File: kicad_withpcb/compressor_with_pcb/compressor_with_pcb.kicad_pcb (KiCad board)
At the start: 2 copper layers, 152.3 x 105 mm, 166 parts, among them J1 EDA 306, Q1 BC549C, Q2 BC549C, Q3 BC549C, Q4 BC549C, Q5 BC549C, Q6 BC549C, Q7 BC549C, Q8 BC549C, Q9 BC549C, SW1 BYPASS, SW2 INT/EXT, SW3 HPF DEFEAT, SW4 LINK, U1 NE5532, U10 LM3915, U2 NE5532, U3 NE5532, U4 TL072, U5 NE5532, U6 NE5532, U7 NE5532, U9 LM3914

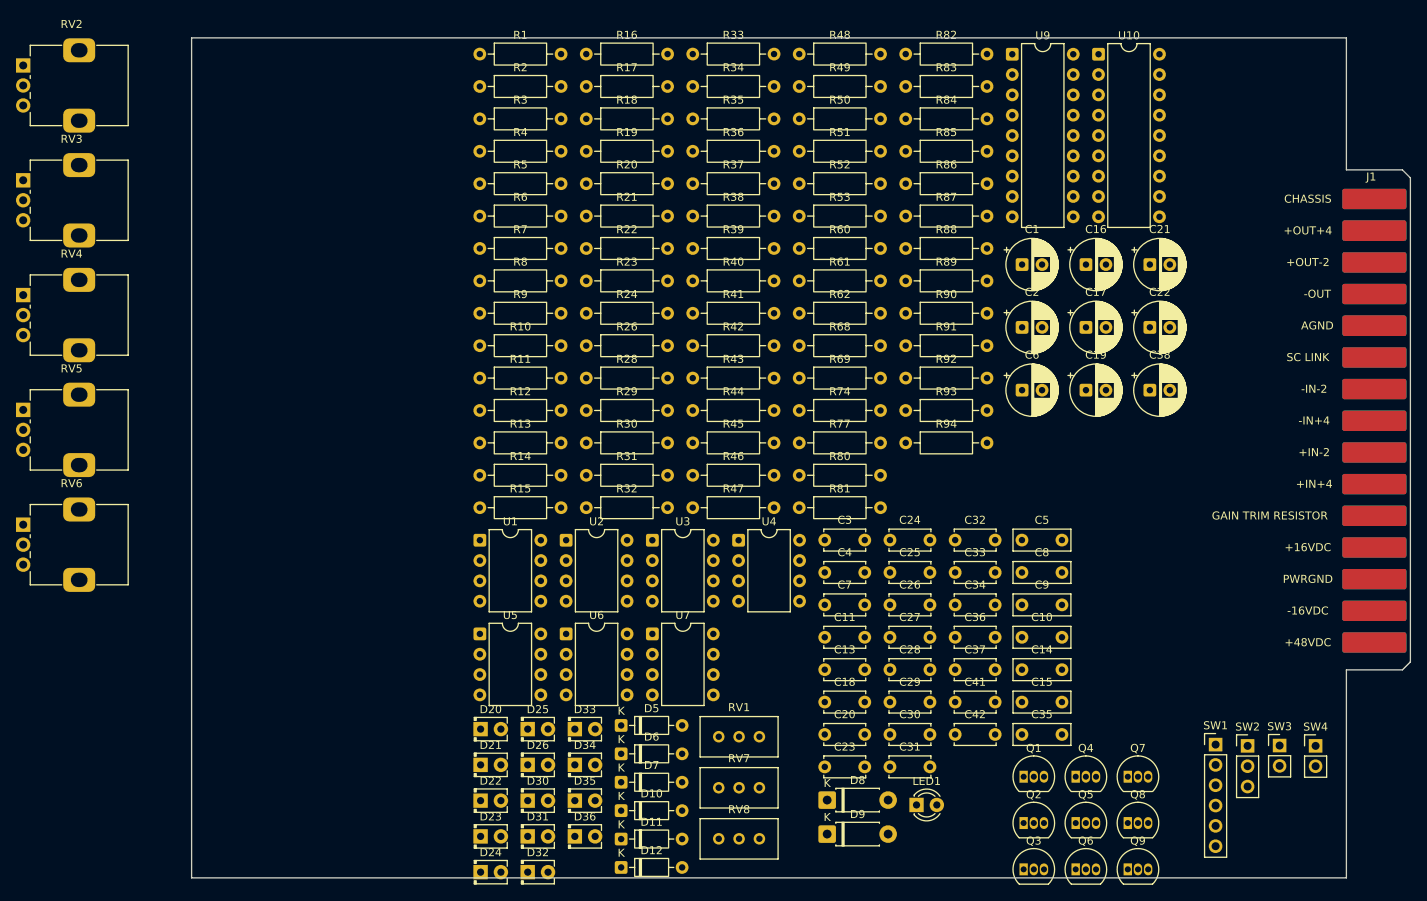
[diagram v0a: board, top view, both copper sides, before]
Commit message: Move panel controls and meters to a front board
Pots, switches and both meters now sit on a separate front board, as the
faceplate fit guide recommends. They stay drawn in the schematic but are
excluded from this board and its BOM. J2 (2x15 IDC) carries the 24 signals
that cross, with ground between the audio pairs.

Front edge set back 24 mm to clear the front board, and the card guide
keep-outs are now 3 mm on both layers.

Co-Authored-By: Claude Opus 5.5 (1M context) <noreply@anthropic.com>
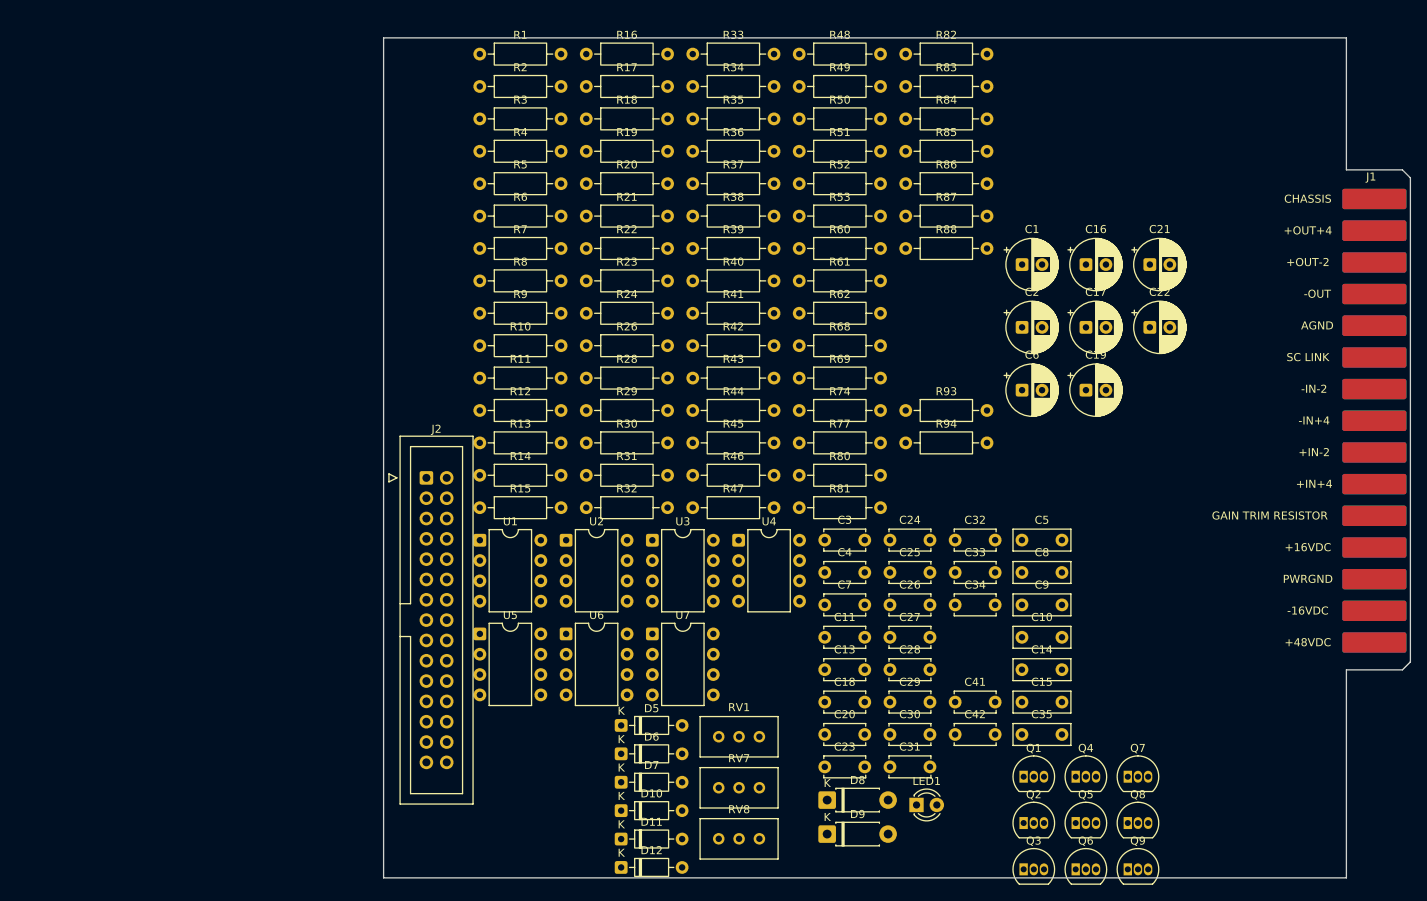
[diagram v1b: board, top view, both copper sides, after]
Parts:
- removed C36, C37: 100n, Capacitor_THT:C_Disc_D5.0mm_W2.5mm_P5.00mm
- removed C38: 47u, Capacitor_THT:CP_Radial_D6.3mm_P2.50mm
- removed D20, D21, D22, D23, D24, D25, D26, D30, D31, D32, D33, D34, D35, D36: meter, LED_THT:LED_D2.0mm_W4.0mm_H2.8mm_FlatTop
- removed R89, R91: 2k7, Resistor_THT:R_Axial_DIN0207_L6.3mm_D2.5mm_P10.16mm_Horizontal
- removed R90, R92: 8k2, Resistor_THT:R_Axial_DIN0207_L6.3mm_D2.5mm_P10.16mm_Horizontal
- removed RV2: 10k, Potentiometer_THT:Potentiometer_Alps_RK09K_Single_Vertical
- removed RV3: 1M, Potentiometer_THT:Potentiometer_Alps_RK09K_Single_Vertical
- removed RV4: 100k, Potentiometer_THT:Potentiometer_Alps_RK09K_Single_Vertical
- removed RV5: 4k7, Potentiometer_THT:Potentiometer_Alps_RK09K_Single_Vertical
- removed RV6: 220k, Potentiometer_THT:Potentiometer_Alps_RK09K_Single_Vertical
- removed SW1: BYPASS, Connector_PinHeader_2.54mm:PinHeader_1x06_P2.54mm_Vertical
- removed SW2: INT/EXT, Connector_PinHeader_2.54mm:PinHeader_1x03_P2.54mm_Vertical
- removed SW3: HPF DEFEAT, Connector_PinHeader_2.54mm:PinHeader_1x02_P2.54mm_Vertical
- removed SW4: LINK, Connector_PinHeader_2.54mm:PinHeader_1x02_P2.54mm_Vertical
- removed U10: LM3915, Package_DIP:DIP-18_W7.62mm
- removed U9: LM3914, Package_DIP:DIP-18_W7.62mm
- added J2: FRONT BOARD, Connector_IDC:IDC-Header_2x15_P2.54mm_Vertical, F.Cu at (80.0, 110.0)
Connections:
- net Net-(D11-K) renamed LVL_METER
- net Net-(D12-K) renamed GR_METER
- net Net-(D7-A) renamed TIMING
- net Net-(R44-Pad1) renamed RATIO_CW
- net Net-(SW3-A) renamed HPF_A
- net Net-(SW3-B) renamed HPF_B
- net Net-(U2A--) renamed MAKEUP_FB
- R28 pad 2: Net-(SW1A-A) -> BYP_A
- R32 pad 2: Net-(SW1B-A) -> BYP_B
- R35 pad 1: Net-(R35-Pad1) -> THR_W
- R45 pad 1: Net-(R45-Pad1) -> RATIO_W
- R45 pad 2: Net-(SW4-A) -> LINK_SW
- R46 pad 1: Net-(R46-Pad1) -> ATK_W
- R47 pad 1: Net-(R47-Pad1) -> REL_W
- R93 pad 1: Net-(U9-REFOUT) -> GR_REF
- U6 pad 5: Net-(SW2-B) -> KEY_SRC
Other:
- board size 152.3 x 105 mm -> 128.3 x 105 mm
- board text added: "Front edge set back 24.0 mm to clear the front board (10 mm pot gap, 1.6 mm board, ribbon header and plug)"

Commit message: Place the main board by section
Power entry by pins 12 to 14, input and output stages next to the fingers,
the gain cell in the middle and the sidechain towards the front with J2.
Decoupling sits against pins 8 and 4 of each op amp, and the matched pair
and quad are placed touching, flat faces together.

Co-Authored-By: Claude Opus 5.5 (1M context) <noreply@anthropic.com>
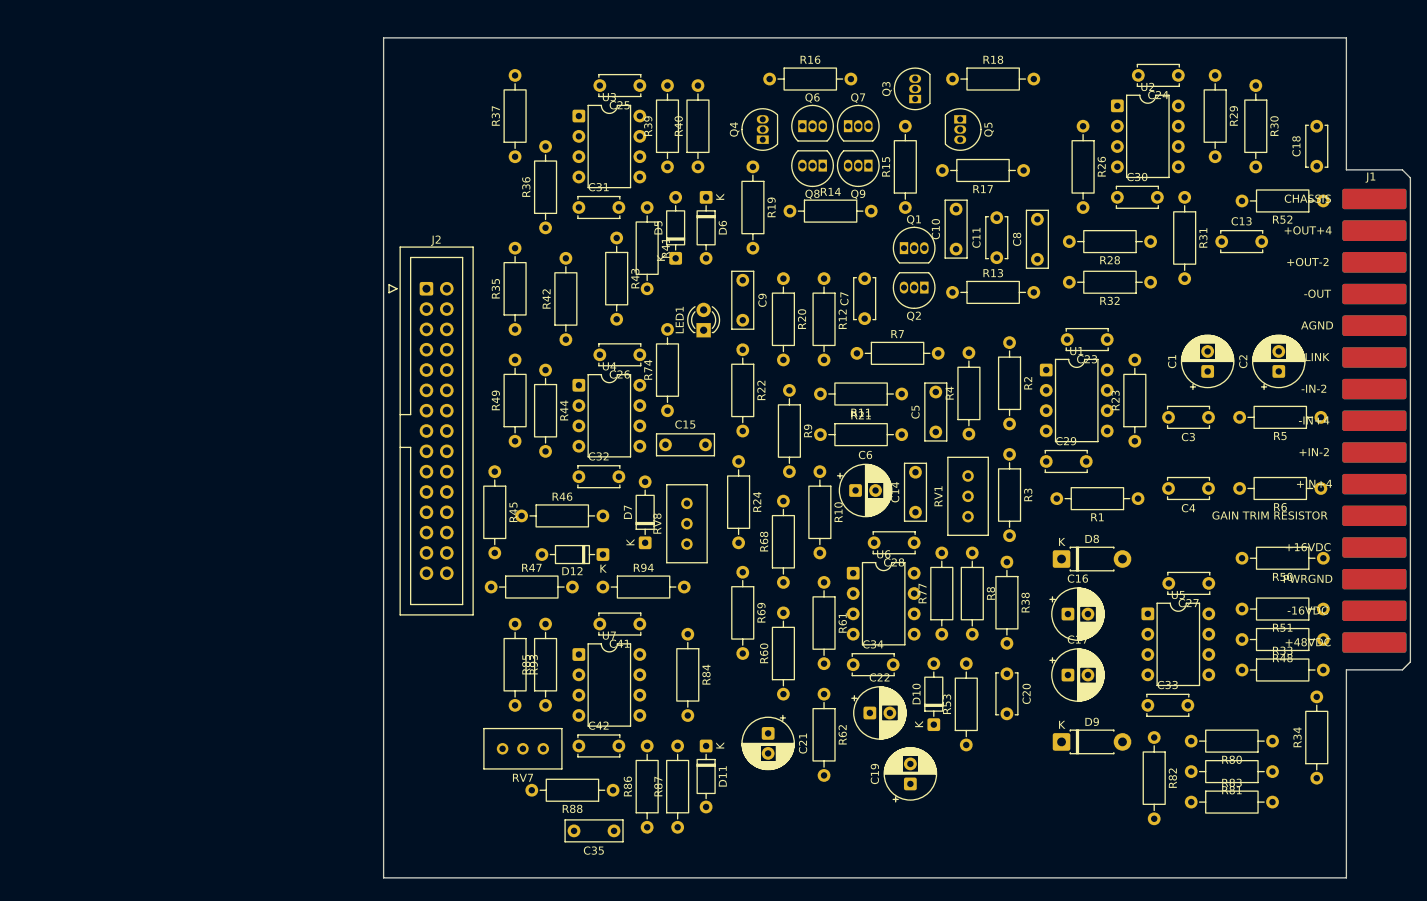
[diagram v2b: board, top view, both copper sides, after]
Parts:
- moved R34 116.4 mm to (191.3, 147.5), turned to 90 degrees
- moved R6 110.5 mm to (191.8, 111.3), turned to 180 degrees
- moved R5 109.1 mm to (191.8, 102.4), turned to 180 degrees
- moved R33 103.2 mm to (182.0, 134.0)
- moved R1 99.3 mm to (169.0, 112.6), turned to 180 degrees
- moved Q6 99.0 mm to (127.0, 66.0)
- moved R48 98.2 mm to (192.1, 130.2), turned to 180 degrees
- moved Q3 97.2 mm to (141.1, 62.6), turned to 90 degrees
- moved R83 96.3 mm to (175.6, 150.5)
- moved R30 94.9 mm to (183.7, 61.0), turned to -90 degrees
- moved Q9 93.7 mm to (135.3, 71.0), turned to 180 degrees
- moved C18 90.9 mm to (191.3, 71.0), turned to 90 degrees
- moved R82 90.9 mm to (171.0, 142.5), turned to -90 degrees
- moved Q8 90.6 mm to (129.5, 71.0), turned to 180 degrees
- moved Q5 89.1 mm to (146.7, 65.2), turned to -90 degrees
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
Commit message: Route the supply rails
+16V, -16V and -5V1 run on the top layer in 0.6 mm from the power entry to
each chip. PGND is a single track from pin 13 to R48, and CHASSIS stays by
pin 1.

Co-Authored-By: Claude Opus 5.5 (1M context) <noreply@anthropic.com>
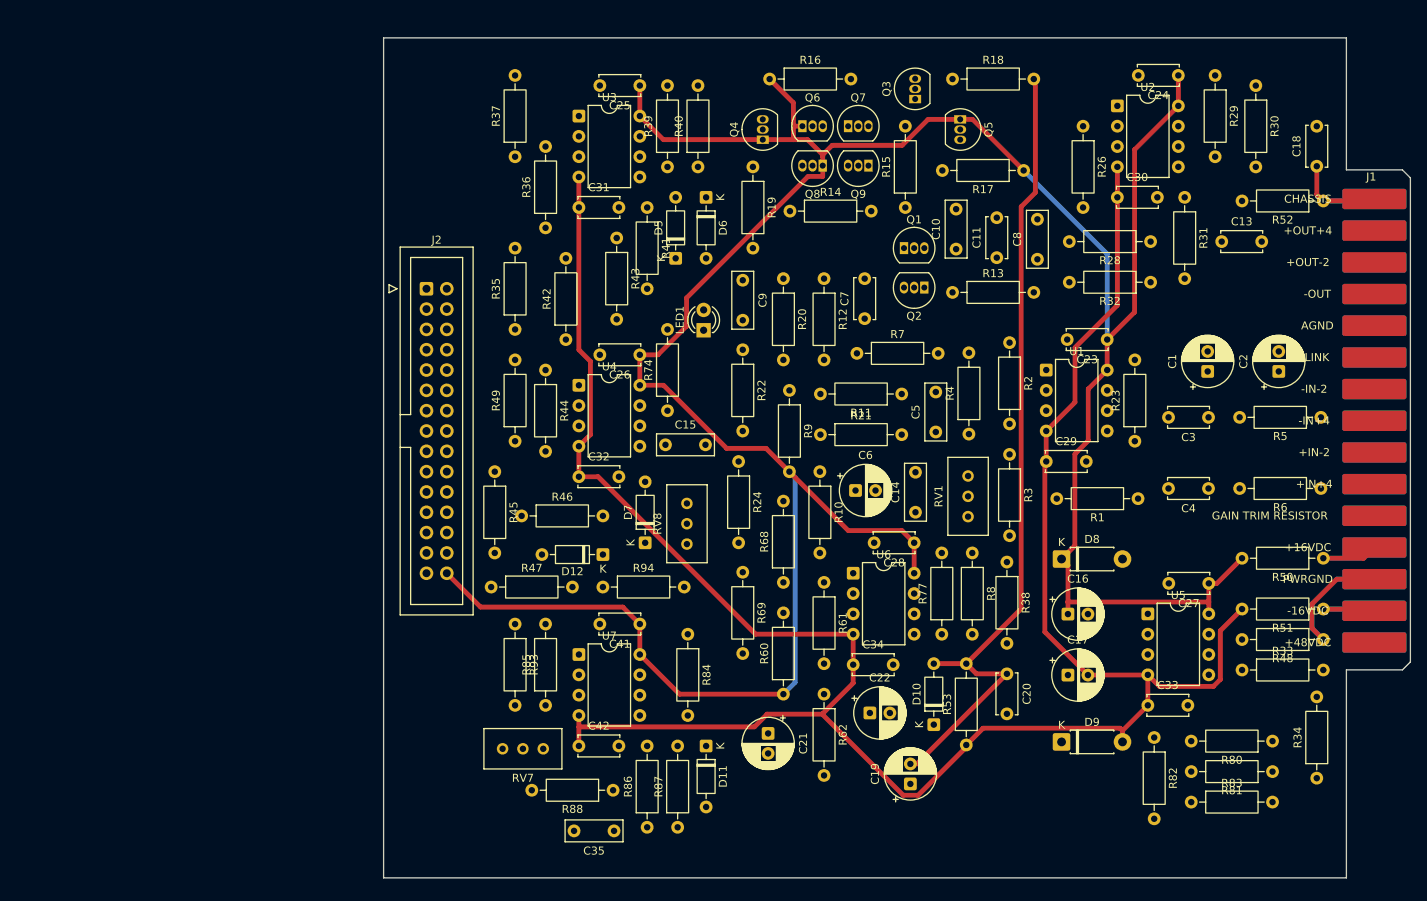
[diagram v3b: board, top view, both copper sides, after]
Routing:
- net +16V: track 0.00 -> 360.5 mm
- net -16V: track 0.00 -> 279.7 mm
- net -5V1: track 0.00 -> 103.1 mm
- net PGND: track 0.00 -> 28.2 mm
- net CHASSIS: track 0.00 -> 17.7 mm
- net +16V-IN: track 0.00 -> 13.9 mm
- net -16V-IN: track 0.00 -> 13.0 mm
